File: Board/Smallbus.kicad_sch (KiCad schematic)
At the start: 2 parts

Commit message: ultipet 1.1a board
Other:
- note added: "CBM-ULTIPET-V1.1A"
- note removed: "CBM-ULTIPET-V1.0A"
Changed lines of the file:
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@@
 		)
 	)
-	(text "CBM-ULTIPET-V1.0A"
+	(text "CBM-ULTIPET-V1.1A"
 		(exclude_from_sim no)
 		(at 152.4 149.86 0)

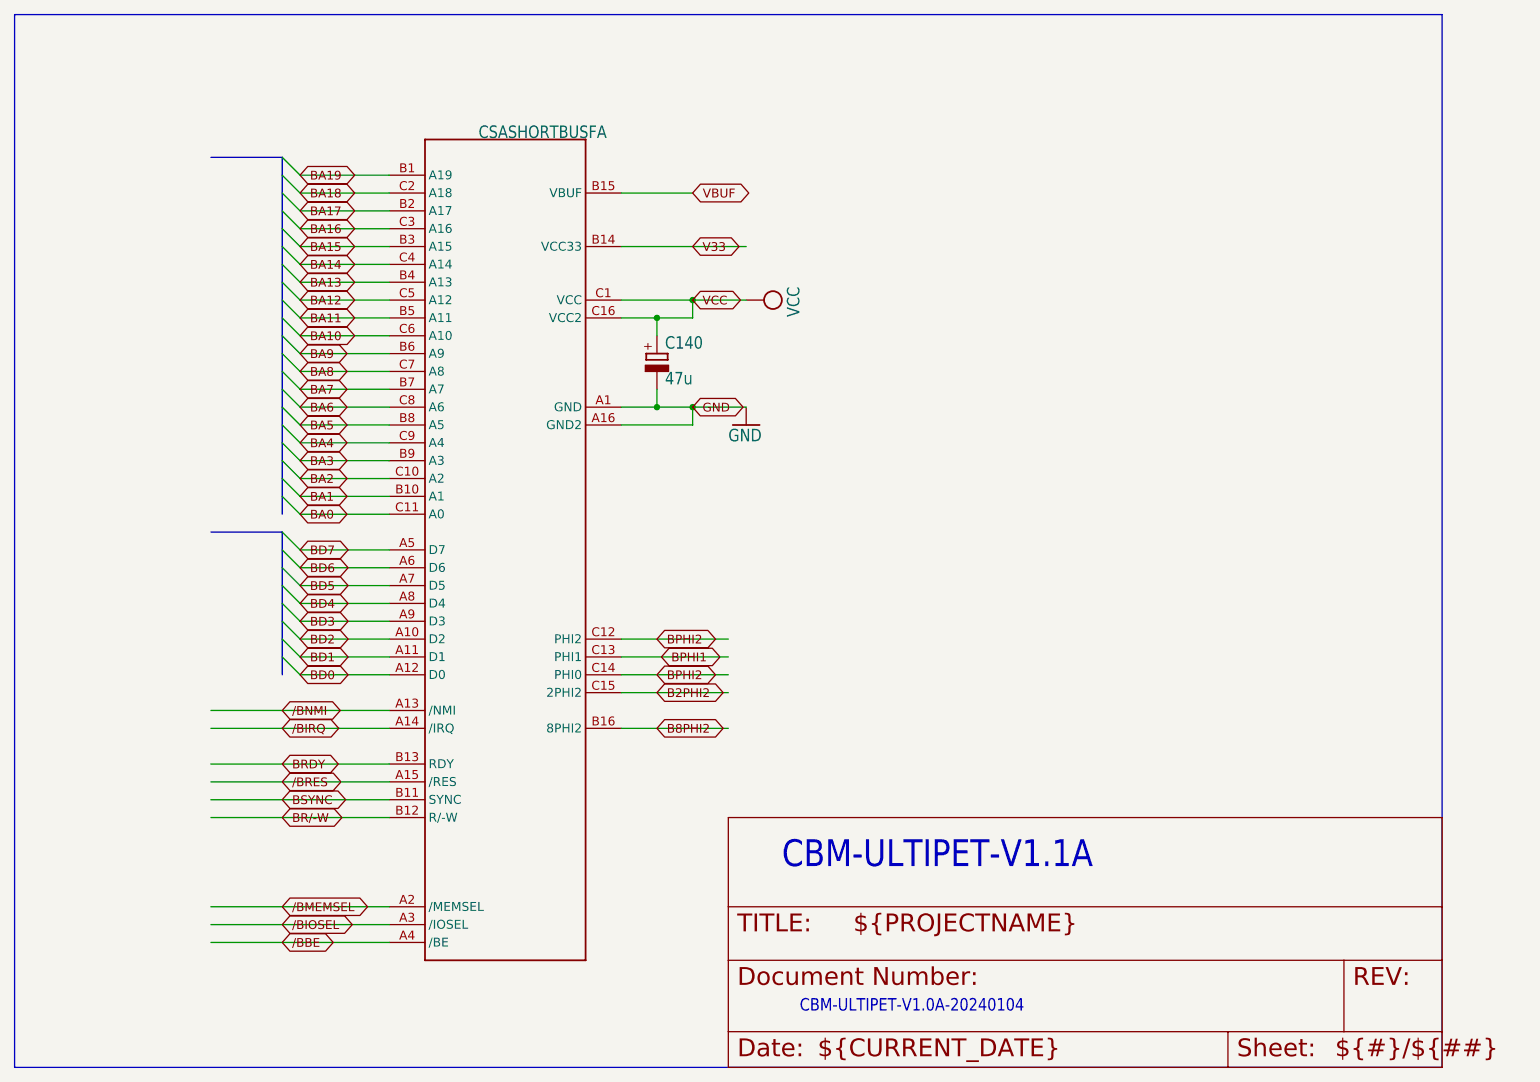
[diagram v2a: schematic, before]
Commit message: clamp diodes for joysticks
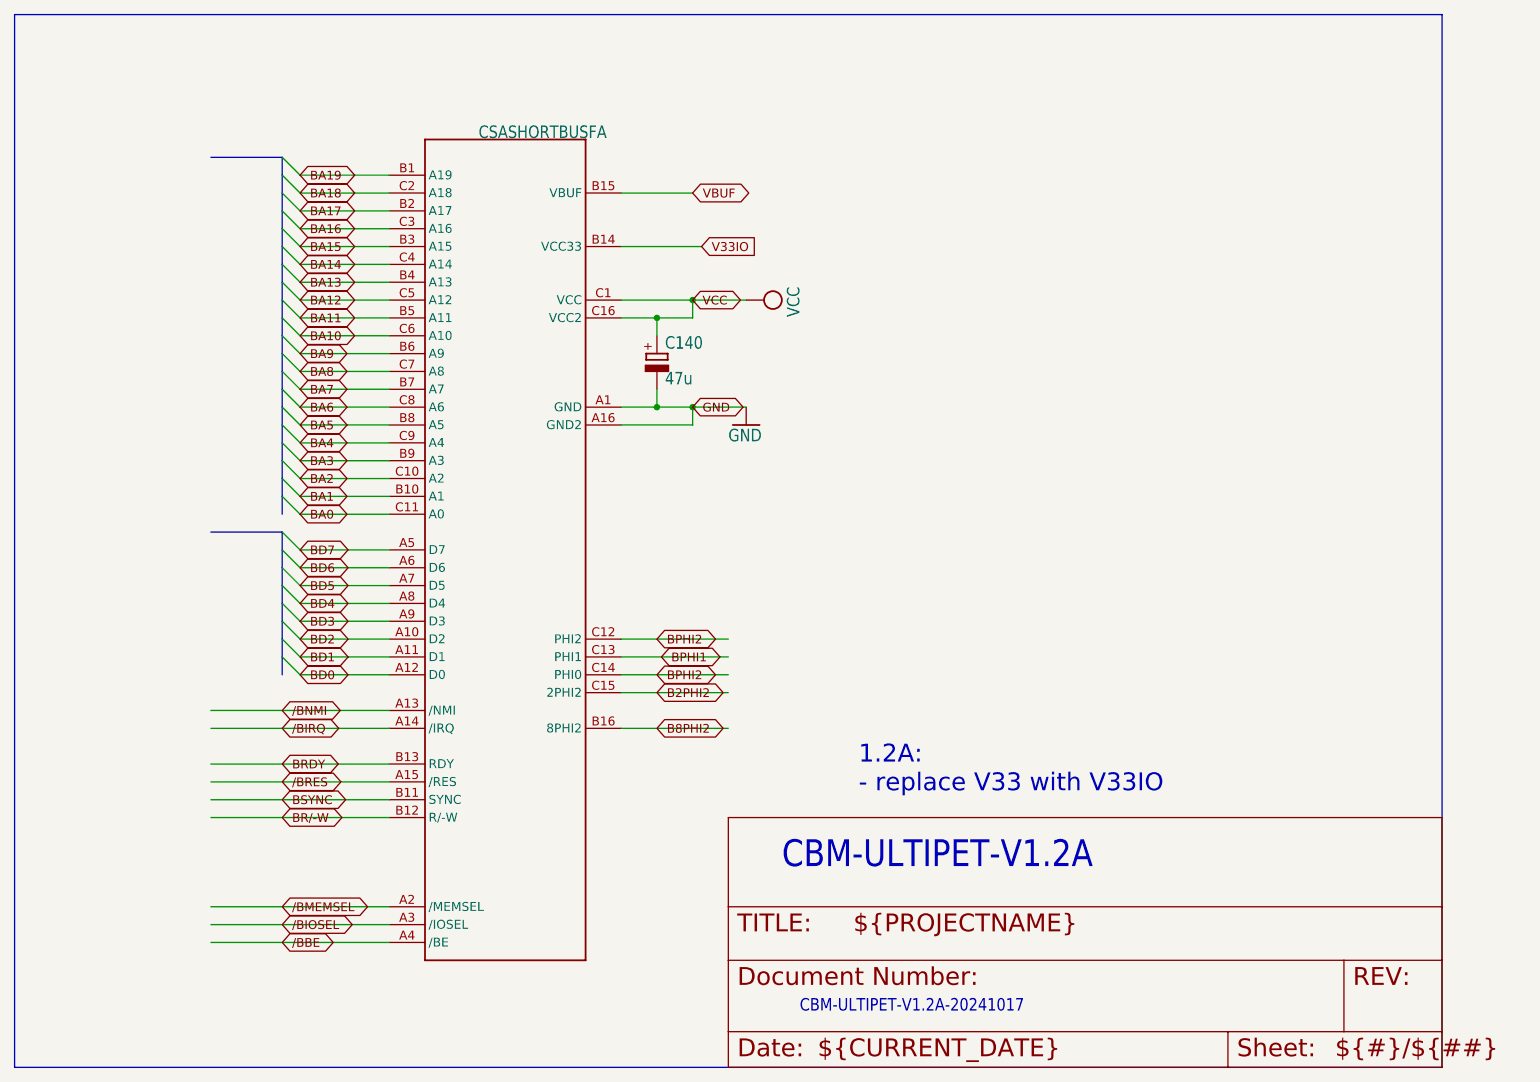
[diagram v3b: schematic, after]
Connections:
- net V33 renamed V33IO
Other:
- note added: "1.2A: - replace V33 with V33IO"
- note added: "CBM-ULTIPET-V1.2A"
- note added: "CBM-ULTIPET-V1.2A-20241017"
- note removed: "CBM-ULTIPET-V1.0A-20240104"
- note removed: "CBM-ULTIPET-V1.1A"
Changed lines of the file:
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@@
-		)
-	)
-	(wire
-		(pts
-			(xy 129.54 60.96) (xy 147.32 60.96)
-		)
-		(stroke
-			(width 0.1524)
-			(type solid)
 		)
 	)
@@
 	(wire
 		(pts
+			(xy 129.54 60.96) (xy 140.97 60.96)
+		)
+		(stroke
+			(width 0)
+			(type default)
+		)
+	)
+	(wire
+		(pts
 			(xy 96.52 139.7) (xy 71.12 139.7)
 		)
@@
 		)
 	)
-	(text "CBM-ULTIPET-V1.1A"
+	(text "CBM-ULTIPET-V1.2A"
 		(exclude_from_sim no)
 		(at 152.4 149.86 0)
@@
 		)
 	)
-	(text "CBM-ULTIPET-V1.0A-20240104"
+	(text "1.2A:\n- replace V33 with V33IO"
+		(exclude_from_sim no)
+		(at 163.322 135.382 0)
+		(effects
+			(font
+				(size 2.54 2.54)
+			)
+			(justify left)
+		)
+	)
+	(text "CBM-ULTIPET-V1.2A-20241017"
 		(exclude_from_sim no)
 		(at 154.94 170.18 0)
@@
 		)
 	)
-	(global_label "V33"
-		(shape bidirectional)
-		(at 139.7 60.96 0)
-		(fields_autoplaced yes)
-		(effects
-			(font
-				(size 1.2446 1.2446)
-			)
-			(justify left)
-		)
-		(property "Intersheetrefs" "${INTERSHEET_REFS}"
-			(at 147.1516 60.96 0)
-			(effects
-				(font
-					(size 1.27 1.27)
-				)
-				(justify left)
-				(hide yes)
-			)
-		)
-	)
 	(global_label "BA8"
 		(shape bidirectional)
@@
 			(effects
 				(font
+					(size 1.27 1.27)
+				)
+				(justify left)
+				(hide yes)
+			)
+		)
+	)
+	(global_label "V33IO"
+		(shape input)
+		(at 140.97 60.96 0)
+		(fields_autoplaced yes)
+		(effects
+			(font
+				(size 1.27 1.27)
+			)
+			(justify left)
+		)
+		(property "Intersheetrefs" "${INTERSHEET_REFS}"
+			(at 149.3981 60.96 0)
+			(effects
+				(font

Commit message: more layout work
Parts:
- added C75: 47u, cbm_ultipet_v1:E2,5-7, symbol cbm_ultipet_v1-eagle-import:CPOL-EUE2.5-7
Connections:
- net GND: now also C75.-
- net V33IO renamed BV33
- net BV33: now also C75.+
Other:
- moved on the sheet: C140
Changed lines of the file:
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@@
+	)
+	(junction
+		(at 133.35 83.82)
+		(diameter 0)
+		(color 0 0 0 0)
 	)
 	(junction
@@
 	)
 	(junction
-		(at 134.62 83.82)
+		(at 161.29 60.96)
 		(diameter 0)
 		(color 0 0 0 0)
 	)
 	(junction
-		(at 134.62 71.12)
+		(at 161.29 83.82)
 		(diameter 0)
 		(color 0 0 0 0)
 	)
+	(junction
+		(at 133.35 71.12)
+		(diameter 0)
+		(color 0 0 0 0)
+	)
+	(junction
+		(at 157.48 83.82)
+		(diameter 0)
+		(color 0 0 0 0)
+	)
 	(bus_entry
 		(at 83.82 50.8)
@@
 	(wire
 		(pts
+			(xy 157.48 83.82) (xy 139.7 83.82)
+		)
+		(stroke
+			(width 0)
+			(type default)
+		)
+	)
+	(wire
+		(pts
 			(xy 96.52 116.84) (xy 83.82 116.84)
 		)
@@
 	(wire
 		(pts
+			(xy 161.29 83.82) (xy 171.45 83.82)
+		)
+		(stroke
+			(width 0.1524)
+			(type solid)
+		)
+	)
+	(wire
+		(pts
 			(xy 96.52 66.04) (xy 83.82 66.04)
 		)
@@
 	(wire
 		(pts
-			(xy 129.54 71.12) (xy 134.62 71.12)
+			(xy 129.54 71.12) (xy 133.35 71.12)
+		)
+		(stroke
+			(width 0.1524)
+			(type solid)
+		)
+	)
+	(wire
+		(pts
+			(xy 157.48 86.36) (xy 157.48 83.82)
+		)
+		(stroke
+			(width 0)
+			(type default)
+		)
+	)
+	(wire
+		(pts
+			(xy 133.35 71.12) (xy 139.7 71.12)
+		)
+		(stroke
+			(width 0.1524)
+			(type solid)
+		)
+	)
+	(wire
+		(pts
+			(xy 133.35 83.82) (xy 139.7 83.82)
 		)
 		(stroke
@@
 		)
 	)
+	(wire
+		(pts
+			(xy 157.48 83.82) (xy 161.29 83.82)
+		)
+		(stroke
+			(width 0.1524)
+			(type solid)
+		)
+	)
 	(bus
 		(pts
@@
 		)
 	)
+	(wire
+		(pts
+			(xy 129.54 60.96) (xy 161.29 60.96)
+		)
+		(stroke
+			(width 0)
+			(type default)
+		)
+	)
 	(bus
 		(pts
@@
 	(wire
 		(pts
-			(xy 129.54 83.82) (xy 134.62 83.82)
+			(xy 129.54 83.82) (xy 133.35 83.82)
 		)
 		(stroke
@@
 	(wire
 		(pts
-			(xy 129.54 60.96) (xy 140.97 60.96)
-		)
-		(stroke
-			(width 0)
-			(type default)
-		)
-	)
-	(wire
-		(pts
 			(xy 96.52 139.7) (xy 71.12 139.7)
 		)
@@
 		)
 	)
-	(wire
-		(pts
-			(xy 134.62 71.12) (xy 139.7 71.12)
-		)
-		(stroke
-			(width 0.1524)
-			(type solid)
-		)
-	)
 	(bus
 		(pts
@@
 		)
 	)
-	(wire
-		(pts
-			(xy 134.62 83.82) (xy 139.7 83.82)
-		)
-		(stroke
-			(width 0.1524)
-			(type solid)
-		)
-	)
 	(bus
 		(pts
@@
 		)
 	)
+	(wire
+		(pts
+			(xy 161.29 60.96) (xy 161.29 71.12)
+		)
+		(stroke
+			(width 0)
+			(type default)
+		)
+	)
 	(polyline
 		(pts
@@
 	(wire
 		(pts
-			(xy 134.62 73.66) (xy 134.62 71.12)
+			(xy 133.35 73.66) (xy 133.35 71.12)
 		)
 		(stroke
@@
 	(wire
 		(pts
+			(xy 161.29 60.96) (xy 167.64 60.96)
+		)
+		(stroke
+			(width 0)
+			(type default)
+		)
+	)
+	(wire
+		(pts
 			(xy 96.52 60.96) (xy 83.82 60.96)
 		)
@@
 		)
 	)
+	(wire
+		(pts
+			(xy 161.29 78.74) (xy 161.29 83.82)
+		)
+		(stroke
+			(width 0)
+			(type default)
+		)
+	)
 	(bus
 		(pts
@@
 	(wire
 		(pts
-			(xy 139.7 83.82) (xy 147.32 83.82)
+			(xy 139.7 83.82) (xy 157.48 83.82)
 		)
 		(stroke
@@
 	(wire
 		(pts
-			(xy 134.62 81.28) (xy 134.62 83.82)
+			(xy 133.35 81.28) (xy 133.35 83.82)
 		)
 		(stroke
@@
 	(global_label "GND"
 		(shape bidirectional)
-		(at 139.7 83.82 0)
-		(fields_autoplaced yes)
-		(effects
-			(font
-				(size 1.2446 1.2446)
-			)
-			(justify left)
-		)
-		(property "Intersheetrefs" "${INTERSHEET_REFS}"
-			(at 147.5073 83.82 0)
+		(at 157.48 86.36 0)
+		(fields_autoplaced yes)
+		(effects
+			(font
+				(size 1.2446 1.2446)
+			)
+			(justify left)
+		)
+		(property "Intersheetrefs" "${INTERSHEET_REFS}"
+			(at 165.2873 86.36 0)
 			(effects
 				(font
@@
 		)
 	)
+	(global_label "BV33"
+		(shape input)
+		(at 167.64 60.96 0)
+		(fields_autoplaced yes)
+		(effects
+			(font
+				(size 1.27 1.27)
+			)
+			(justify left)
+		)
+		(property "Intersheetrefs" "${INTERSHEET_REFS}"
+			(at 175.4028 60.96 0)
+			(effects
+				(font
+					(size 1.27 1.27)
+				)
+				(justify left)
+				(hide yes)
+			)
+		)
+	)
 	(global_label "BD5"
 		(shape bidirectional)
@@
 		(property "Intersheetrefs" "${INTERSHEET_REFS}"
 			(at 91.5087 116.84 0)
-			(effects
-				(font
-					(size 1.27 1.27)
-				)
-				(justify left)
-				(hide yes)
-			)
-		)
-	)
-	(global_label "V33IO"
-		(shape input)
-		(at 140.97 60.96 0)
-		(fields_autoplaced yes)
-		(effects
-			(font
-				(size 1.27 1.27)
-			)
-			(justify left)
-		)
-		(property "Intersheetrefs" "${INTERSHEET_REFS}"
-			(at 149.3981 60.96 0)
 			(effects
 				(font
@@
 	(symbol
 		(lib_id "cbm_ultipet_v1-eagle-import:CPOL-EUE2.5-7")
-		(at 134.62 76.2 0)
+		(at 133.35 76.2 0)
 		(unit 1)
 		(exclude_from_sim no)
@@
 		(dnp no)
 		(property "Reference" "C140"
-			(at 135.763 75.7174 0)
+			(at 134.493 75.7174 0)
 			(effects
 				(font
@@
 		)
 		(property "Value" "47u"
-			(at 135.763 80.7974 0)
+			(at 134.493 80.7974 0)
 			(effects
 				(font
@@
 		)
 		(property "Footprint" "cbm_ultipet_v1:E2,5-7"
-			(at 134.62 76.2 0)
+			(at 133.35 76.2 0)
 			(effects
 				(font
@@
 		)
 		(property "Datasheet" ""
-			(at 134.62 76.2 0)
+			(at 133.35 76.2 0)
 			(effects
 				(font
@@
 		)
 		(property "Description" ""
-			(at 134.62 76.2 0)
+			(at 133.35 76.2 0)
 			(effects
 				(font
@@
 				(path "/4dd2dd78-173f-4b46-8cce-4ed940435c94/5525398a-a941-4dda-a276-d843e4519a96"
 					(reference "C140")
+					(unit 1)
+				)
+			)
+		)
+	)
+	(symbol
+		(lib_id "cbm_ultipet_v1-eagle-import:CPOL-EUE2.5-7")
+		(at 161.29 73.66 0)
+		(unit 1)
+		(exclude_from_sim no)
+		(in_bom yes)
+		(on_board yes)
+		(dnp no)
+		(property "Reference" "C75"
+			(at 162.433 73.1774 0)
+			(effects
+				(font
+					(size 1.778 1.5113)
+				)
+				(justify left bottom)
+			)
+		)
+		(property "Value" "47u"
+			(at 162.433 78.2574 0)
+			(effects
+				(font
+					(size 1.778 1.5113)
+				)
+				(justify left bottom)
+			)
+		)
+		(property "Footprint" "cbm_ultipet_v1:E2,5-7"
+			(at 161.29 73.66 0)
+			(effects
+				(font
+					(size 1.27 1.27)
+				)
+				(hide yes)
+			)
+		)
+		(property "Datasheet" ""
+			(at 161.29 73.66 0)
+			(effects
+				(font
+					(size 1.27 1.27)
+				)
+				(hide yes)
+			)
+		)
+		(property "Description" ""
+			(at 161.29 73.66 0)
+			(effects
+				(font
+					(size 1.27 1.27)
+				)
+				(hide yes)
+			)
+		)
+		(pin "+"
+		)
+		(pin "-"
+		)
+		(instances
+			(project "cbm_ultipet_v1"
+				(path "/4dd2dd78-173f-4b46-8cce-4ed940435c94/5525398a-a941-4dda-a276-d843e4519a96"
+					(reference "C75")
 					(unit 1)
 				)
@@
 	(symbol
 		(lib_id "cbm_ultipet_v1-eagle-import:GND")
-		(at 147.32 86.36 0)
+		(at 171.45 86.36 0)
 		(unit 1)
 		(exclude_from_sim no)
@@
 		(dnp no)
 		(property "Reference" "#GND059"
-			(at 147.32 86.36 0)
+			(at 171.45 86.36 0)
 			(effects
 				(font
@@
 		)
 		(property "Value" "GND"
-			(at 144.78 88.9 0)
+			(at 168.91 88.9 0)
 			(effects
 				(font
@@
 		)
 		(property "Footprint" ""
-			(at 147.32 86.36 0)
+			(at 171.45 86.36 0)
 			(effects
 				(font
@@
 		)
 		(property "Datasheet" ""
-			(at 147.32 86.36 0)
+			(at 171.45 86.36 0)
 			(effects
 				(font
@@
 		)
 		(property "Description" ""
-			(at 147.32 86.36 0)
-			(effects
-				(font
+			(at 171.45 86.36 0)
+			(effects
+				(font

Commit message: first work on r1.3
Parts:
- U$25: footprint cbm_ultipet_v1:FABC48R2 -> Footprints:FABC48R2-reversed
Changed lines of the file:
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@@
 			)
 		)
-		(property "Footprint" "cbm_ultipet_v1:FABC48R2"
+		(property "Footprint" "Footprints:FABC48R2-reversed"
 			(at 114.3 104.14 0)
 			(effects

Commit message: preview for r1.3
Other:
- note added: "1.2A: - replace V33 with V33IO 1.3A: - correct (mirrored) pinout"
- note added: "CBM-ULTIPET-V1.3A"
- note added: "CBM-ULTIPET-V1.3A-20250806"
- note removed: "1.2A: - replace V33 with V33IO"
- note removed: "CBM-ULTIPET-V1.2A"
- note removed: "CBM-ULTIPET-V1.2A-20241017"
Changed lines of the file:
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@@
 	(generator_version "9.0")
 	(paper "A4")
-	(text "CBM-ULTIPET-V1.2A"
+	(text "CBM-ULTIPET-V1.3A"
 		(exclude_from_sim no)
 		(at 152.4 149.86 0)
@@
 		)
 	)
-	(text "1.2A:\n- replace V33 with V33IO"
+	(text "1.2A:\n- replace V33 with V33IO\n1.3A:\n- correct (mirrored) pinout"
 		(exclude_from_sim no)
-		(at 163.322 135.382 0)
+		(at 169.164 130.556 0)
 		(effects
 			(font
@@
 		)
 	)
-	(text "CBM-ULTIPET-V1.2A-20241017"
+	(text "CBM-ULTIPET-V1.3A-20250806"
 		(exclude_from_sim no)
 		(at 154.94 170.18 0)

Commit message: rename U refs to UX*
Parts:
- renumbered U$25 to UX25
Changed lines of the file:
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@@
 		(on_board yes)
 		(dnp no)
-		(property "Reference" "U$25"
+		(property "Reference" "UX25"
 			(at 114.3 114.3 90)
 			(effects
@@
 			(project "cbm_ultipet_v1"
 				(path "/4dd2dd78-173f-4b46-8cce-4ed940435c94/5525398a-a941-4dda-a276-d843e4519a96"
-					(reference "U$25")
+					(reference "UX25")
 					(unit 1)
 				)
